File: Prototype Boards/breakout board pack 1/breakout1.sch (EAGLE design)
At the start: 14 parts, among them IC1 74LS151D, IC2 74LS03D, Q1 BCX70SMD

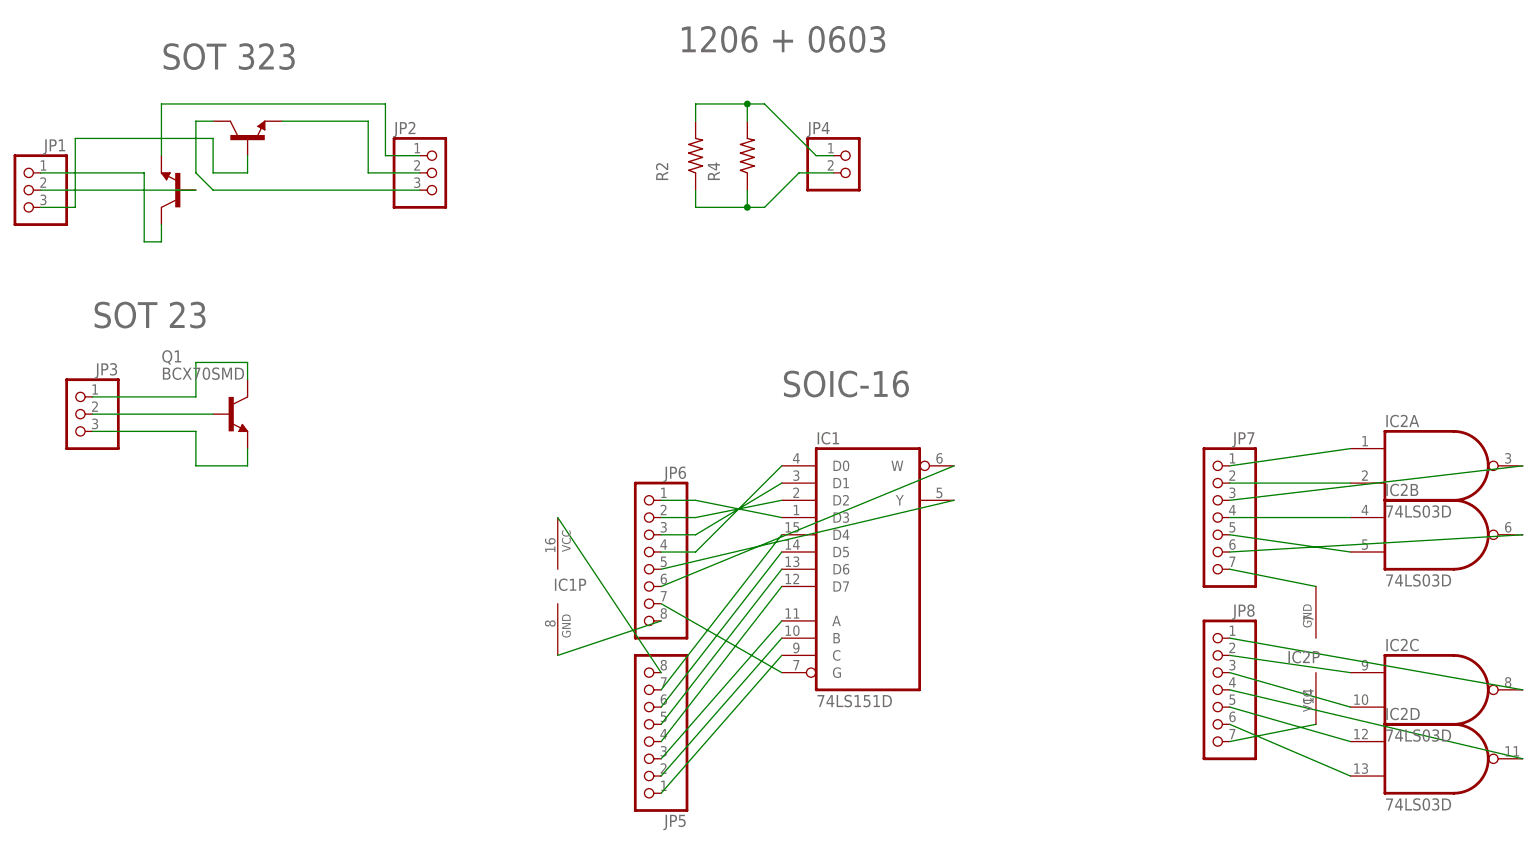
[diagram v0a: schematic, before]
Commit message: finished laying out the breakout board. going to order this soon.
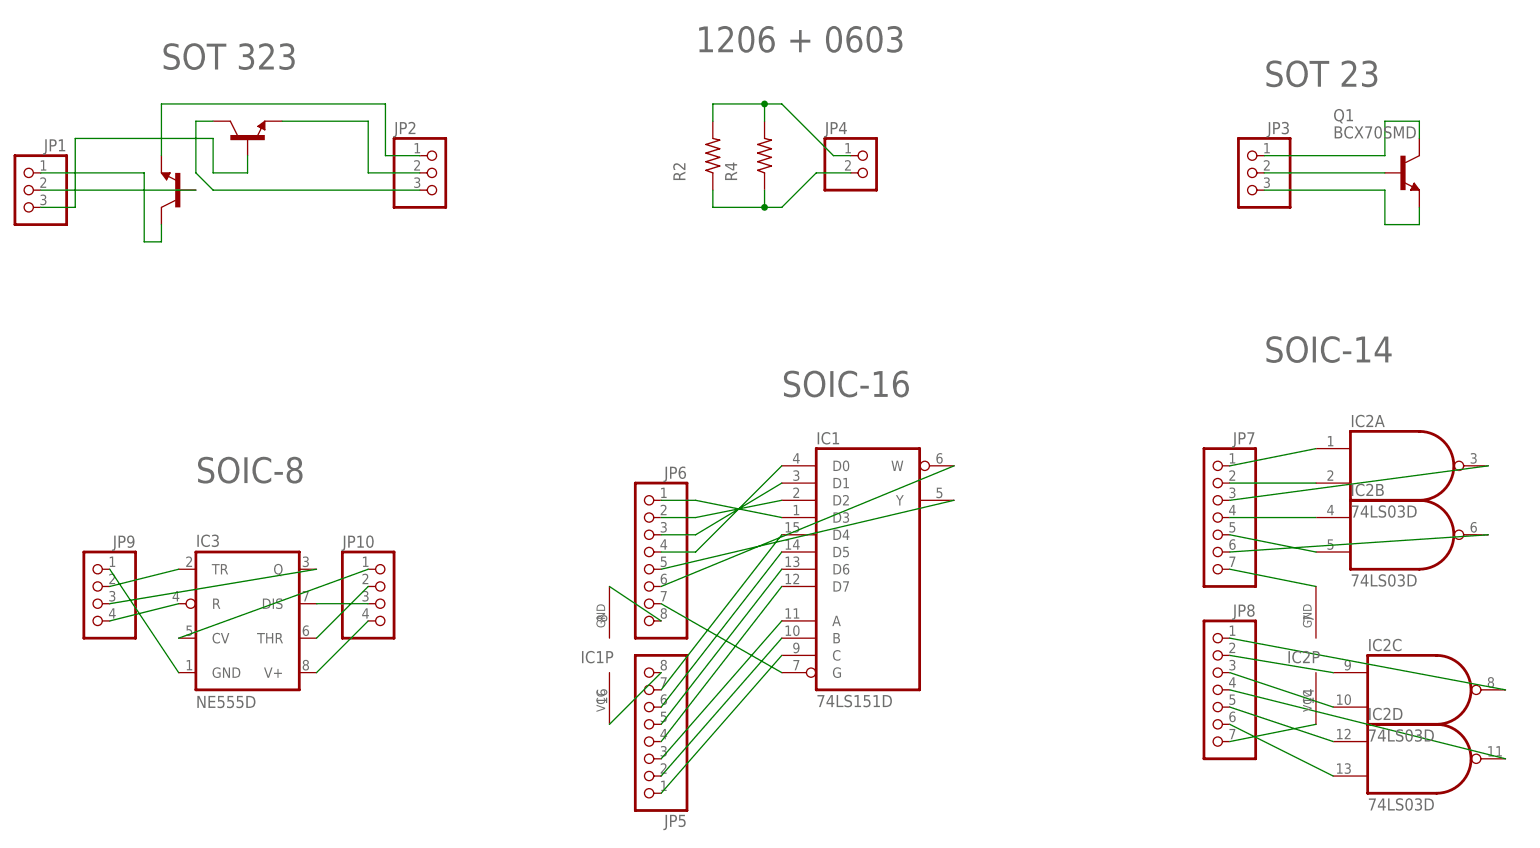
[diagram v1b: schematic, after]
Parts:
- added IC3: NE555D, linear:NE555D
- added JP10, JP9: (no value), pinhead:PINHD-1X4
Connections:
- new net N$44: IC3.GND, JP9.1
- new net N$45: IC3.TR, JP9.2
- new net N$46: IC3.R, JP9.4
- new net N$47: IC3.Q, JP9.3
- new net N$48: IC3.CV, JP10.1
- new net N$49: IC3.THR, JP10.2
- new net N$50: IC3.DIS, JP10.3
- new net N$51: IC3.V+, JP10.4
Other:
- note added: "SOIC-14"
- note added: "SOIC-8"
- moved on the sheet: IC1P, IC2A, IC2B, IC2C, IC2D, JP3, JP4, Q1, R2, R4
